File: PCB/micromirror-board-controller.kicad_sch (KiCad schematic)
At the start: 25 parts, among them J1 Barrel_Jack, J2 Conn_01x04_Female, J3 Conn_01x03_Female, J4 Conn_2Rows-51Pins, J5 Conn_01x02_Pin, J6 USB_C_Receptacle_USB2.0, SW1 SW_Push, SW2 SW_Push, U1 Pico, U2 LM1117IMPX-5.0

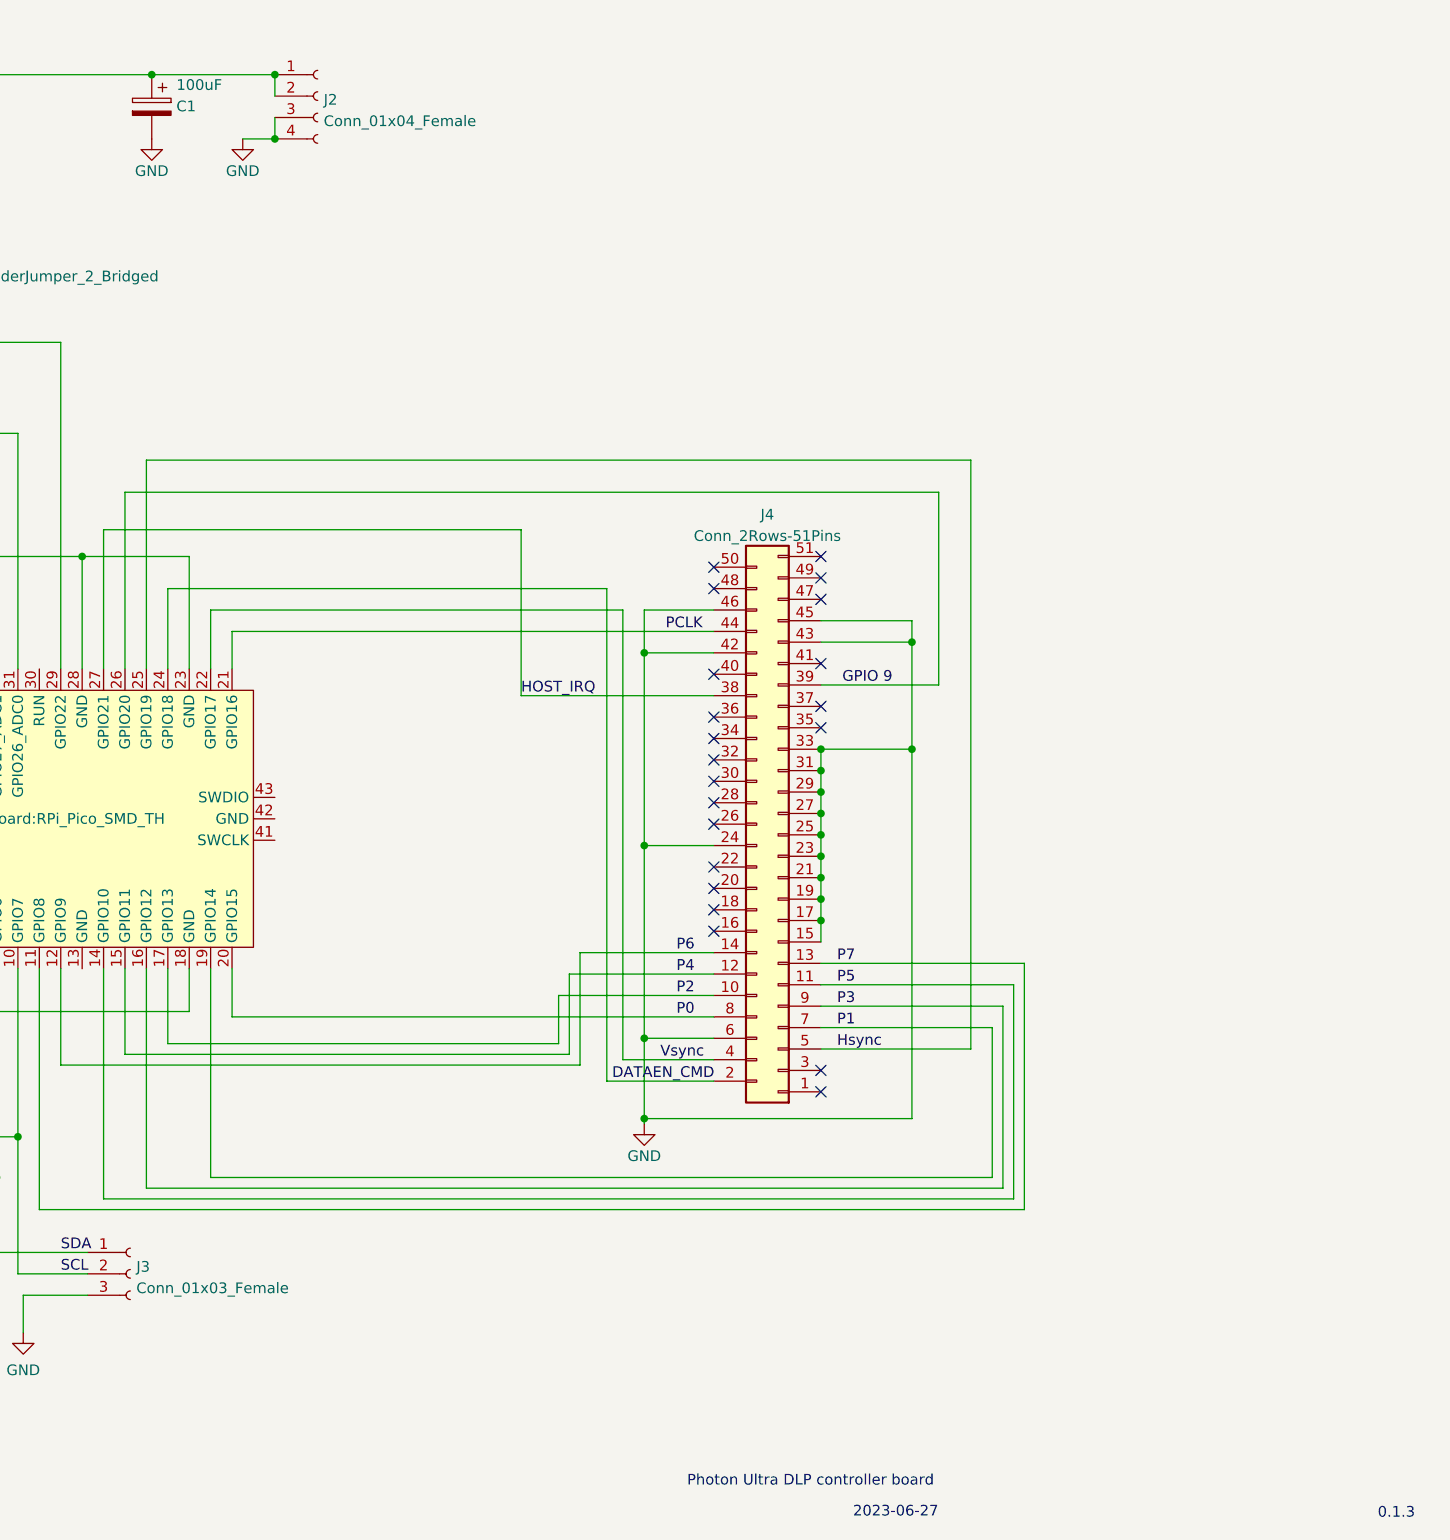
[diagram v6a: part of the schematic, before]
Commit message: Fix +12V pinout and revise board
Fixed the 12V board pinout (apparently GND and VSUP are swapped).  Some early code on talking to the DLPC1438; not all verified to be correct yet.
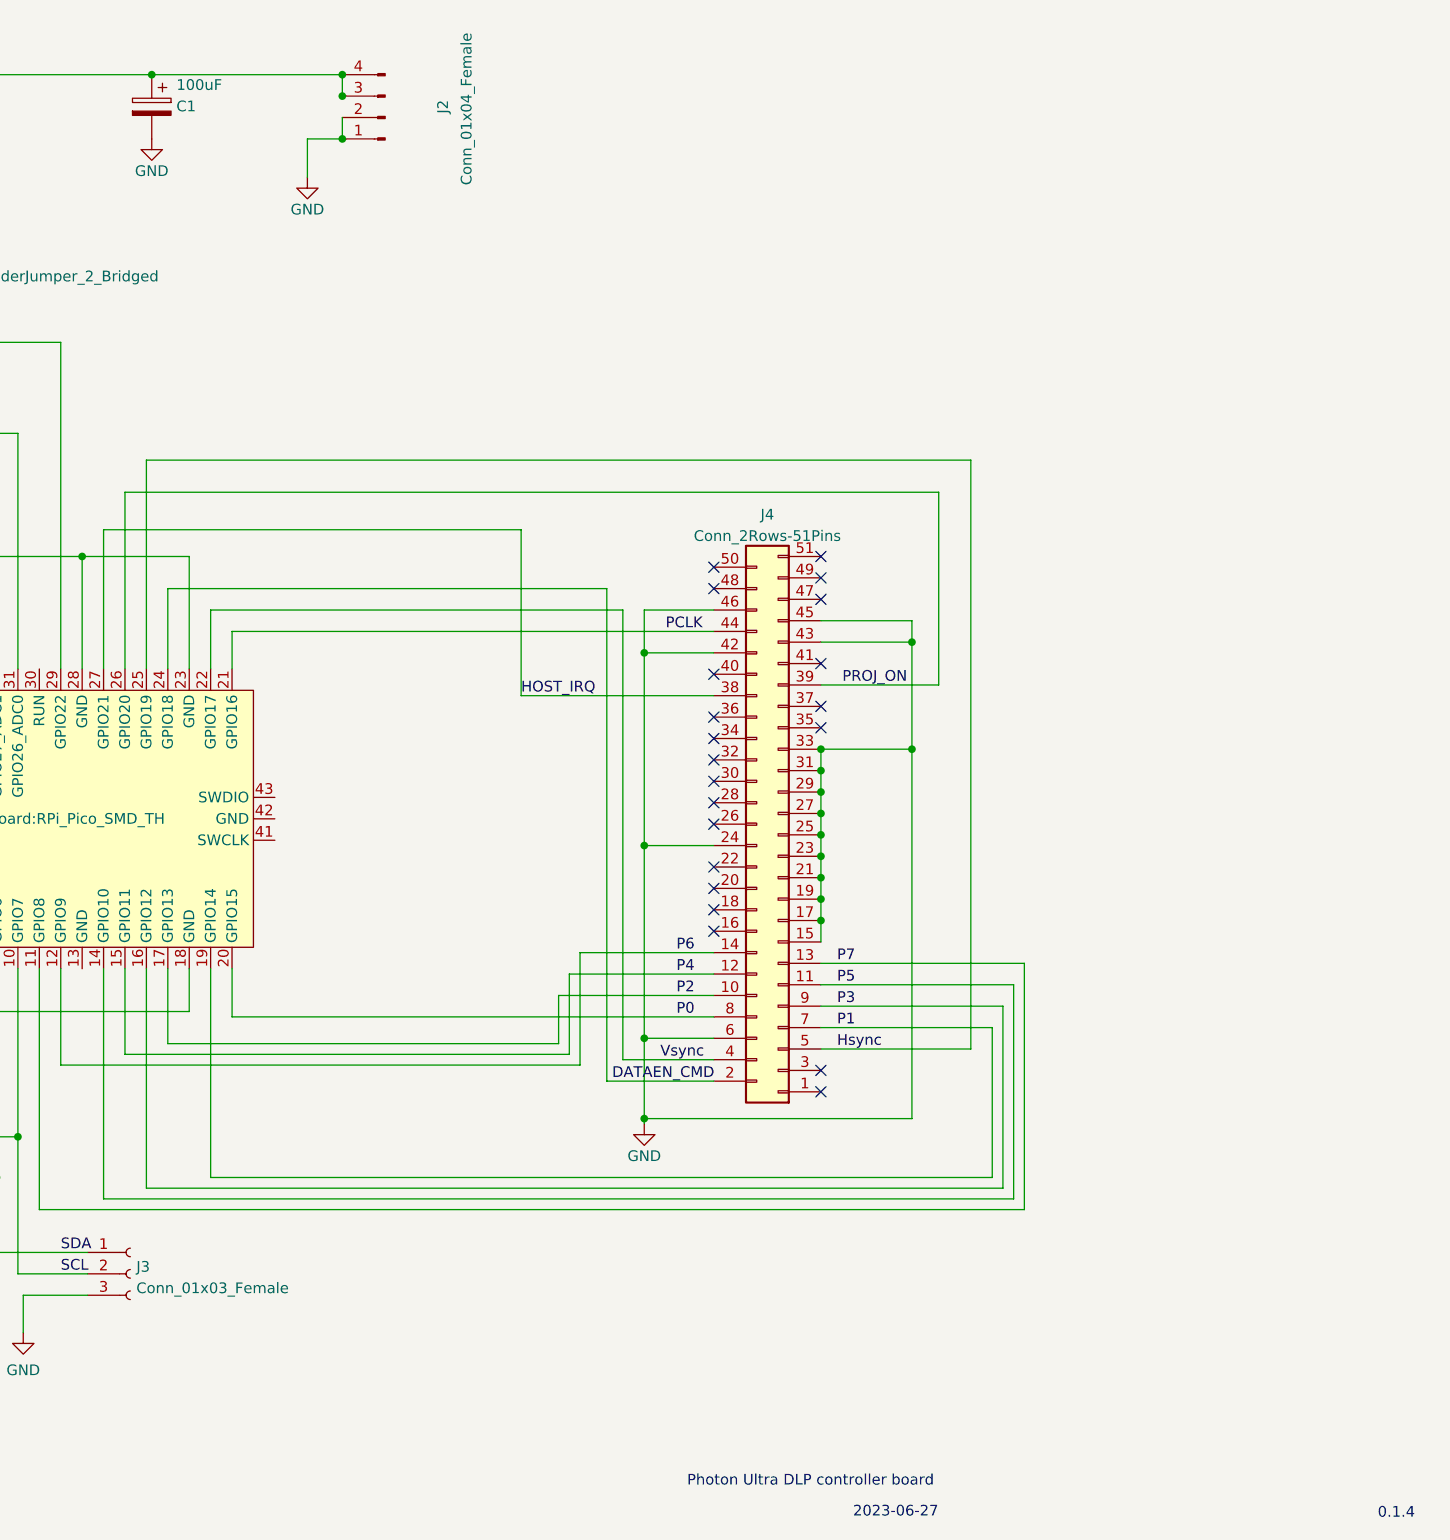
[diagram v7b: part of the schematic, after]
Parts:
- J2: symbol Connector:Conn_01x04_Female -> Connector:Conn_01x04_Pin
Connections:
- net +12V: now also J2.3 (Pin_3), J2.4 (Pin_4); no longer J2.1 (Pin_1), J2.2 (Pin_2)
- net GND: now also J2.1 (Pin_1), J2.2 (Pin_2); no longer J2.3 (Pin_3), J2.4 (Pin_4)
- net GPIO 9 renamed PROJ_ON
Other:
- note added: "0.1.4"
- note removed: "0.1.3"
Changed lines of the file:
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@@
   (junction (at 86.995 74.295) (diameter 0) (color 0 0 0 0)
   )
-  (junction (at 137.795 30.48) (diameter 0) (color 0 0 0 0)
+  (junction (at 145.796 30.48) (diameter 0) (color 0 0 0 0)
   )
   (junction (at 73.025 32.385) (diameter 0) (color 0 0 0 0)
@@
   (junction (at 181.61 137.16) (diameter 0) (color 0 0 0 0)
   )
+  (junction (at 145.796 22.86) (diameter 0) (color 0 0 0 0)
+  )
   (junction (at 100.965 48.895) (diameter 0) (color 0 0 0 0)
   )
@@
   (junction (at 202.565 115.57) (diameter 0) (color 0 0 0 0)
   )
-  (junction (at 137.795 22.86) (diameter 0) (color 0 0 0 0)
-  )
   (junction (at 202.565 118.11) (diameter 0) (color 0 0 0 0)
   )
@@
   )
   (junction (at 202.565 107.95) (diameter 0) (color 0 0 0 0)
+  )
+  (junction (at 145.796 25.4) (diameter 0) (color 0 0 0 0)
   )
   (no_connect (at 202.565 140.97))
@@
     (stroke (width 0) (type default))
   )
+  (wire (pts (xy 145.796 30.48) (xy 141.6527 30.48))
+    (stroke (width 0) (type default))
+  )
   (wire (pts (xy 226.695 157.48) (xy 226.695 128.27))
     (stroke (width 0) (type default))
@@
     (stroke (width 0) (type default))
   )
-  (wire (pts (xy 137.795 27.94) (xy 137.795 30.48))
+  (wire (pts (xy 123.19 22.86) (xy 145.796 22.86))
     (stroke (width 0) (type default))
   )
@@
     (stroke (width 0) (type default))
   )
-  (wire (pts (xy 137.795 22.86) (xy 137.795 25.4))
-    (stroke (width 0) (type default))
-  )
   (wire (pts (xy 181.61 114.3) (xy 181.61 137.16))
     (stroke (width 0) (type default))
@@
     (stroke (width 0) (type default))
   )
-  (wire (pts (xy 123.19 22.86) (xy 137.795 22.86))
+  (wire (pts (xy 145.796 22.86) (xy 145.796 25.4))
     (stroke (width 0) (type default))
   )
@@
     (stroke (width 0) (type default))
   )
-  (wire (pts (xy 133.985 30.48) (xy 137.795 30.48))
-    (stroke (width 0) (type default))
-  )
   (wire (pts (xy 202.565 120.65) (xy 202.565 118.11))
     (stroke (width 0) (type default))
@@
     (stroke (width 0) (type default))
   )
+  (wire (pts (xy 145.796 27.94) (xy 145.796 30.48))
+    (stroke (width 0) (type default))
+  )
   (wire (pts (xy 88.392 148.844) (xy 95.25 148.844))
     (stroke (width 0) (type default))
@@
     (stroke (width 0) (type default))
   )
+  (wire (pts (xy 145.796 25.4) (xy 145.796 25.654))
+    (stroke (width 0) (type default))
+  )
   (wire (pts (xy 86.995 74.295) (xy 81.28 74.295))
     (stroke (width 0) (type default))
@@
   )
   (wire (pts (xy 107.315 128.905) (xy 107.315 148.844))
+    (stroke (width 0) (type default))
+  )
+  (wire (pts (xy 141.6527 30.48) (xy 141.6527 35.0454))
     (stroke (width 0) (type default))
   )
@@
     (effects (font (size 1.27 1.27)) (justify left bottom))
   )
-  (text "0.1.3\n" (at 268.605 194.31 0)
+  (text "0.1.4\n" (at 268.605 194.31 0)
     (effects (font (size 1.27 1.27)) (justify left bottom))
   )
@@
     (effects (font (size 1.27 1.27)) (justify left bottom))
   )
-  (label "GPIO 9" (at 205.105 95.25 0) (fields_autoplaced)
+  (label "PROJ_ON" (at 205.105 95.25 0) (fields_autoplaced)
     (effects (font (size 1.27 1.27)) (justify left bottom))
   )
@@
     )
   )
-  (symbol (lib_name "GND_7") (lib_id "power:GND") (at 133.985 30.48 0) (unit 1)
-    (in_bom yes) (on_board yes) (dnp no)
-    (property "Reference" "#PWR0104" (at 133.985 36.83 0)
-      (effects (font (size 1.27 1.27)) hide)
-    )
-    (property "Value" "GND" (at 133.985 34.29 0)
-      (effects (font (size 1.27 1.27)))
-    )
-    (property "Footprint" "" (at 133.985 30.48 0)
-      (effects (font (size 1.27 1.27)) hide)
-    )
-    (property "Datasheet" "" (at 133.985 30.48 0)
+  (symbol (lib_name "GND_7") (lib_id "power:GND") (at 141.6527 35.0454 0) (unit 1)
+    (in_bom yes) (on_board yes) (dnp no)
+    (property "Reference" "#PWR0104" (at 141.6527 41.3954 0)
+      (effects (font (size 1.27 1.27)) hide)
+    )
+    (property "Value" "GND" (at 141.6527 38.8554 0)
+      (effects (font (size 1.27 1.27)))
+    )
+    (property "Footprint" "" (at 141.6527 35.0454 0)
+      (effects (font (size 1.27 1.27)) hide)
+    )
+    (property "Datasheet" "" (at 141.6527 35.0454 0)
       (effects (font (size 1.27 1.27)) hide)
     )
@@
     )
   )
-  (symbol (lib_id "Connector:Conn_01x04_Female") (at 142.875 25.4 0) (unit 1)
-    (in_bom yes) (on_board yes) (dnp no) (fields_autoplaced)
-    (property "Reference" "J2" (at 143.5862 25.8353 0)
-      (effects (font (size 1.27 1.27)) (justify left))
-    )
-    (property "Value" "Conn_01x04_Female" (at 143.5862 28.3722 0)
-      (effects (font (size 1.27 1.27)) (justify left))
-    )
-    (property "Footprint" "Connector_JST:JST_PH_B4B-PH-SM4-TB_1x04-1MP_P2.00mm_Vertical" (at 142.875 25.4 0)
-      (effects (font (size 1.27 1.27)) hide)
-    )
-    (property "Datasheet" "~" (at 142.875 25.4 0)
-      (effects (font (size 1.27 1.27)) hide)
-    )
-    (property "Mouser" "https://nl.mouser.com/ProductDetail/Adafruit/4390?qs=xZ%2FP%252Ba9zWqaq7Vo4%2FzdP%252BA%3D%3D" (at 142.875 25.4 0)
-      (effects (font (size 1.27 1.27)) hide)
-    )
+  (symbol (lib_id "Connector:Conn_01x04_Pin") (at 150.876 27.94 180) (unit 1)
+    (in_bom yes) (on_board yes) (dnp no)
+    (property "Reference" "J2" (at 157.734 26.67 90)
+      (effects (font (size 1.27 1.27)))
+    )
+    (property "Value" "Conn_01x04_Female" (at 160.528 26.924 90)
+      (effects (font (size 1.27 1.27)))
+    )
+    (property "Footprint" "Connector_JST:JST_PH_B4B-PH-SM4-TB_1x04-1MP_P2.00mm_Vertical" (at 150.876 27.94 0)
+      (effects (font (size 1.27 1.27)) hide)
+    )
+    (property "Datasheet" "~" (at 150.876 27.94 0)
+      (effects (font (size 1.27 1.27)) hide)
+    )
+    (property "Mouser" "https://nl.mouser.com/ProductDetail/Adafruit/4390?qs=xZ%2FP%252Ba9zWqaq7Vo4%2FzdP%252BA%3D%3D" (at 150.876 27.94 0)
+      (effects (font (size 1.27 1.27)) hide)
+    )

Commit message: Update source files
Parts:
- J4: Mouser https://nl.mouser.com/ProductDetail/Hirose-Connector/FH35C-51S-0.3SHW99?qs=zPSbg0dgZojGf7NOzFerhQ%3D%3D -> https://nl.mouser.com/ProductDetail/Hirose-Connector/FH35C-51S-0.3SHW50?qs=zPSbg0dgZogQHnwinvS01w%3D%3D; Mouser-id (none) -> 798-FH35C51S03SHW50
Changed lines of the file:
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@@
       (effects (font (size 1.27 1.27)) hide)
     )
-    (property "Mouser" "https://nl.mouser.com/ProductDetail/Hirose-Connector/FH35C-51S-0.3SHW99?qs=zPSbg0dgZojGf7NOzFerhQ%3D%3D" (at 197.485 113.03 0)
+    (property "Mouser" "https://nl.mouser.com/ProductDetail/Hirose-Connector/FH35C-51S-0.3SHW50?qs=zPSbg0dgZogQHnwinvS01w%3D%3D" (at 197.485 113.03 0)
       (effects (font (size 1.27 1.27)) hide)
     )
+    (property "Mouser-id" "798-FH35C51S03SHW50" (at 197.485 113.03 0)
+      (effects (font (size 1.27 1.27)) hide)
+    )
